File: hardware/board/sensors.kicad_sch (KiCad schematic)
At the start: 21 parts, among them U52 MXC6655XA, U53 AK09918C, U54 SC7A20TR_C5126709, U55 ICM-20600, U56 STK3311-X_C966926, U57 HAL248TDSO

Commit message: finished schematic!
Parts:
- added C371: 100nF X5R 10V, Capacitor_SMD:C_0201_0603Metric, symbol Device:C
- added R218, R219: 2.2K 5%, Resistor_SMD:R_0402_1005Metric, symbol Device:R
- added U1: RK3568, RK3568:BGA636C65P28X28_1900X1900X168, symbol RK3568:RK3568
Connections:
- net ALPS_INT_L_GPIO2_D3: now also U1.AC7 (GPIO2_D3_D); no longer U57.3 (OUT)
- net GND: now also C371.2
- net GSENSOR_INT_L_GPIO2_D2: now also U1.AC8 (GPIO2_D2_D)
- net GYRO_INT_L_GPIO2_D4: now also U1.AF5 (GPIO2_D4_D)
- net I2C5_SCL_M0: now also R219.2, U1.AF1 (GPIO3_B3_D)
- net I2C5_SDA_M0: now also R218.2, U1.AE1 (GPIO3_B4_D)
- net VCC_1V8 renamed VCCIO5
- net VCCIO5: now also C371.1, R218.1, R219.1, U1.V10 (VCCIO5), U1.V11 (VCCIO5)
- new net BQ_OTG_EN_H_GPIO3_C3: U1.AC4 (GPIO3_C3_D)
- new net HALL_INT_L_GPIO0_C6: U57.3 (OUT)
- new net HP_DET_L_GPIO3_C2: U1.AA7 (GPIO3_C2_D)
- new net LCD_EN_H_GPIO2_D5: U1.AF6 (GPIO2_D5_D)
- new net LCD_RST_L_GPIO2_D6: U1.AD6 (GPIO2_D6_D)
- new net PCIE20_CLKREQn_M1: U1.AG6 (GPIO2_D0_D)
- new net PCIE20_PERSTn_M1: U1.AD1 (GPIO3_C1_D)
- new net PCIE20_WAKEn_M1: U1.AD7 (GPIO2_D1_D)
- no-connect marks 14 -> 32
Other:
- moved on the sheet: C328, C329, C330, C331, C332, C333, R177, R178, R179, U55, U56, U57

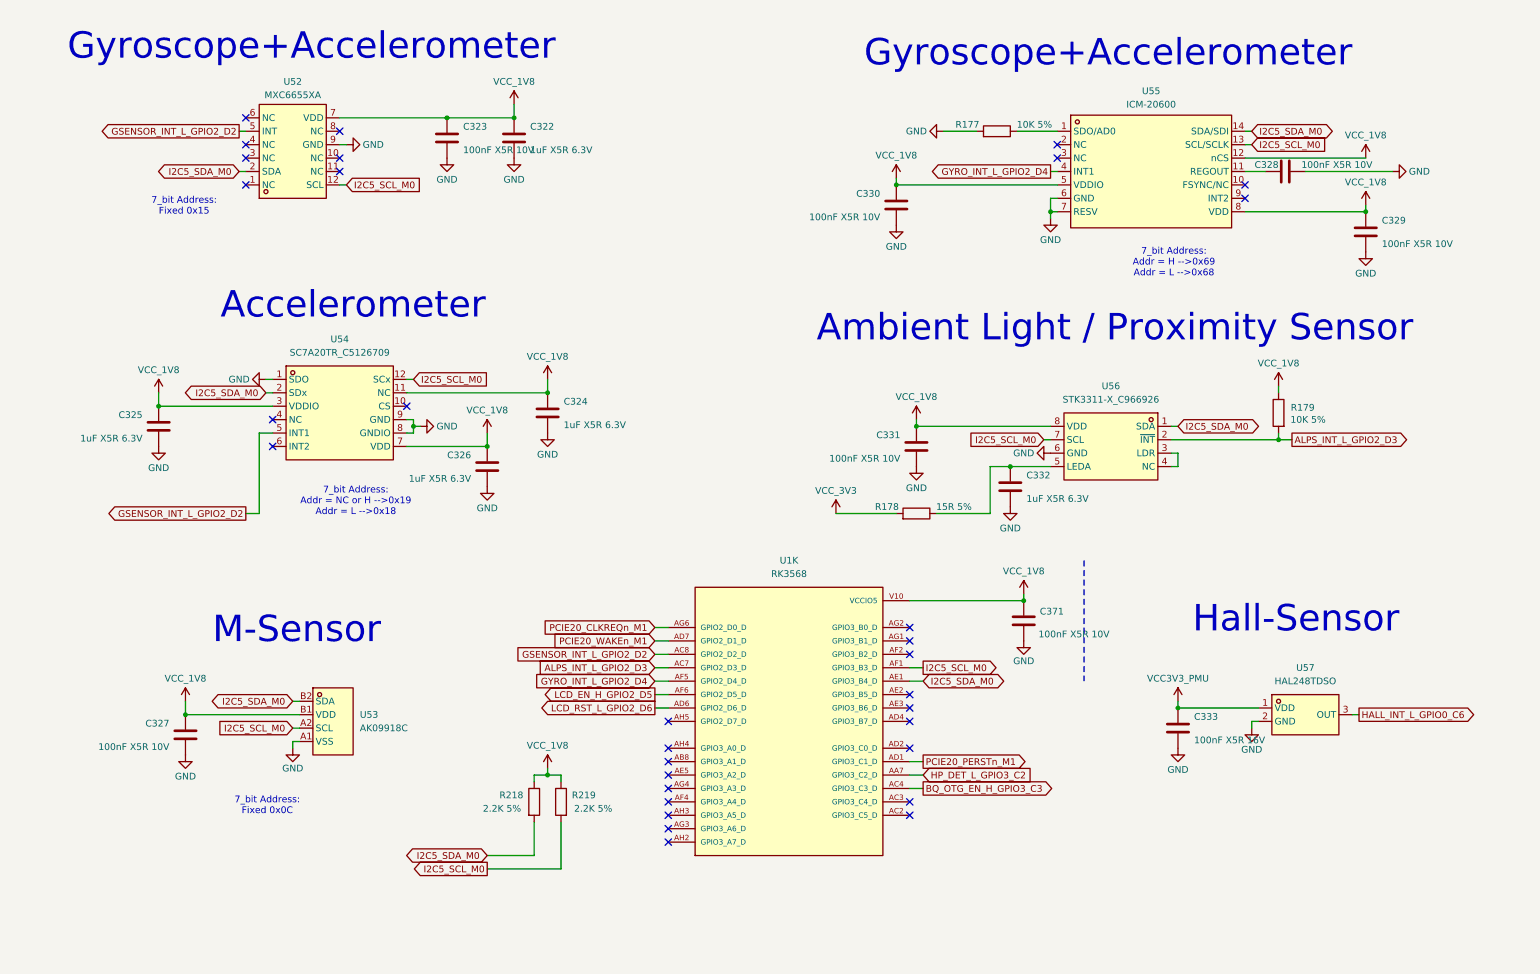
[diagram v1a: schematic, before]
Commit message: finished beautifying schematic
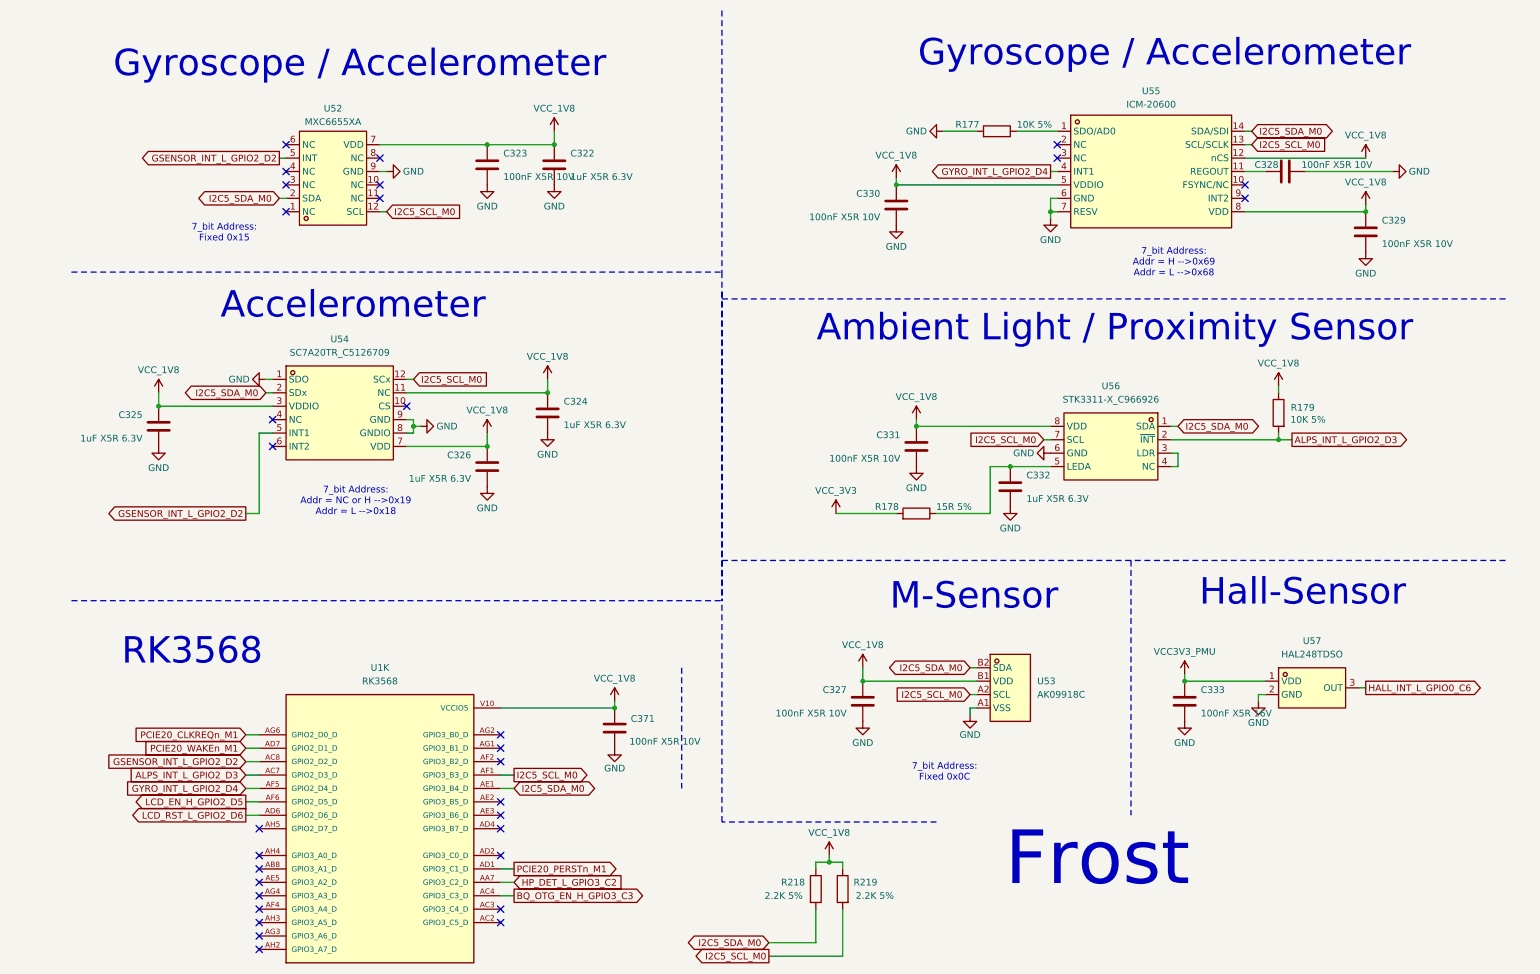
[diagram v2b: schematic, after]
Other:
- note added: "Frost"
- note added: "Gyroscope / Accelerometer"
- note added: "RK3568"
- note removed: "Gyroscope+Accelerometer"
- moved on the sheet: C322, C323, C327, C333, C371, R218, R219, U1K, U52, U53, U57
